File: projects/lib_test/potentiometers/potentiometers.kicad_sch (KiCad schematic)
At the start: 3 parts, among them P1001 500R, P1002 2k, P1003 5k

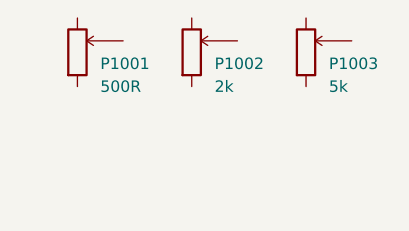
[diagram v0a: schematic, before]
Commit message: add potmeter 1k PTV09 series
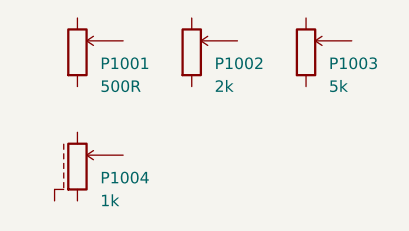
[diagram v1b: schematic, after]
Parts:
- added P1004: 1k, lily_footprints:pot_ptv09a_4025f, symbol lily_symbols:pot_lin_1k_20%_50mW_ptv09a-4025f

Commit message: add potmeter scale silkscreen
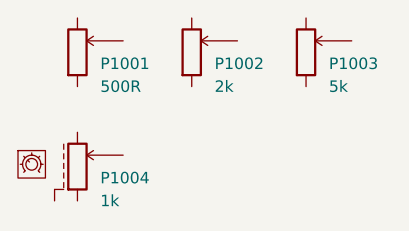
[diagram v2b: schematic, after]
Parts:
- added DOC1001: doc_pot_meter_scale_18mm_280deg_15pos_min_max, lily_footprints:doc_pot_meter_scale_18mm_280deg_15pos_min_max, symbol lily_symbols:doc_pot_meter_scale_18mm_280deg_15pos_min_max
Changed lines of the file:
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@@
+	)
+	(symbol
+		(lib_id "lily_symbols:doc_pot_meter_scale_18mm_280deg_15pos_min_max")
+		(at 20.32 43.18 0)
+		(unit 1)
+		(body_style 1)
+		(exclude_from_sim yes)
+		(in_bom no)
+		(on_board yes)
+		(in_pos_files no)
+		(dnp no)
+		(property "Reference" "DOC1001"
+			(at 20.32 48.26 0)
+			(hide yes)
+			(show_name no)
+			(do_not_autoplace no)
+			(effects
+				(font
+					(size 1.27 1.27)
+				)
+			)
+		)
+		(property "Value" "doc_pot_meter_scale_18mm_280deg_15pos_min_max"
+			(at 20.32 45.72 0)
+			(hide yes)
+			(show_name no)
+			(do_not_autoplace no)
+			(effects
+				(font
+					(size 1.27 1.27)
+				)
+			)
+		)
+		(property "Footprint" "lily_footprints:doc_pot_meter_scale_18mm_280deg_15pos_min_max"
+			(at 20.32 53.34 0)
+			(hide yes)
+			(show_name no)
+			(do_not_autoplace no)
+			(effects
+				(font
+					(size 1.27 1.27)
+				)
+			)
+		)
+		(property "Datasheet" ""
+			(at 20.32 43.18 0)
+			(hide yes)
+			(show_name no)
+			(do_not_autoplace no)
+			(effects
+				(font
+					(size 1.27 1.27)
+				)
+			)
+		)
+		(property "Description" ""
+			(at 20.32 43.18 0)
+			(hide yes)
+			(show_name no)
+			(do_not_autoplace no)
+			(effects
+				(font
+					(size 1.27 1.27)
+				)
+			)
+		)
+		(property "Revision" "1"
+			(at 20.32 50.8 0)
+			(hide yes)
+			(show_name no)
+			(do_not_autoplace no)
+			(effects
+				(font
+					(size 1.27 1.27)
+				)
+			)
+		)
+		(instances
+			(project "potentiometers"
+				(path "/e63e39d7-6ac0-4ffd-8aa3-1841a4541b55"
+					(reference "DOC1001")
+					(unit 1)
+				)
+			)
+		)
 	)
 	(symbol
